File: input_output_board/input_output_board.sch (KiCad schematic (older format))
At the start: 23 parts, among them J1 Neutrik_NCJ6FA-H, J2 Neutrik_NCJ6FA-H, J3 Neutrik_NCJ6FA-H, J4 Neutrik_NCJ6FA-H, J5 AudioJack3, J6 Conn_02x05_Odd_Even, J7 Molex_SL_01x04_Male, J8 Molex_SL_01x04_Male, K1 G6S-2, K2 G6S-2, K3 G6S-2, K4 G6S-2, K5 G6S-2

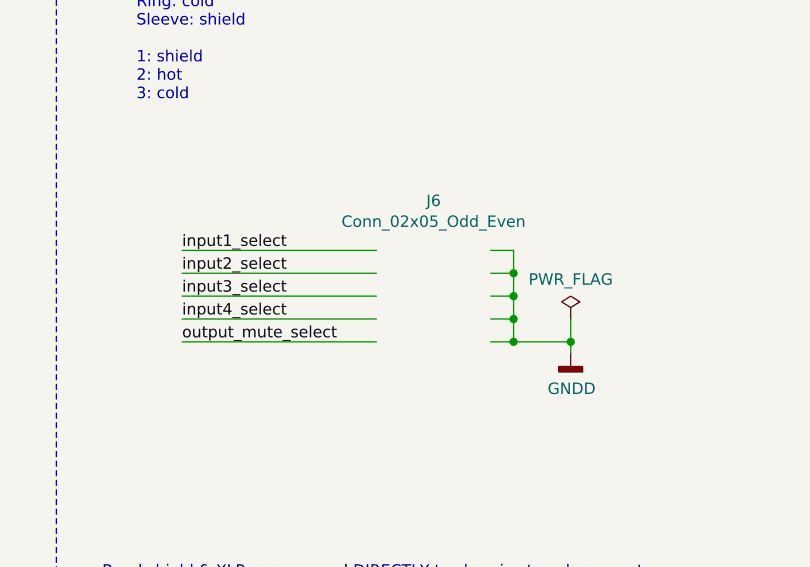
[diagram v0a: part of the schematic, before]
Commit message: complete initial layout
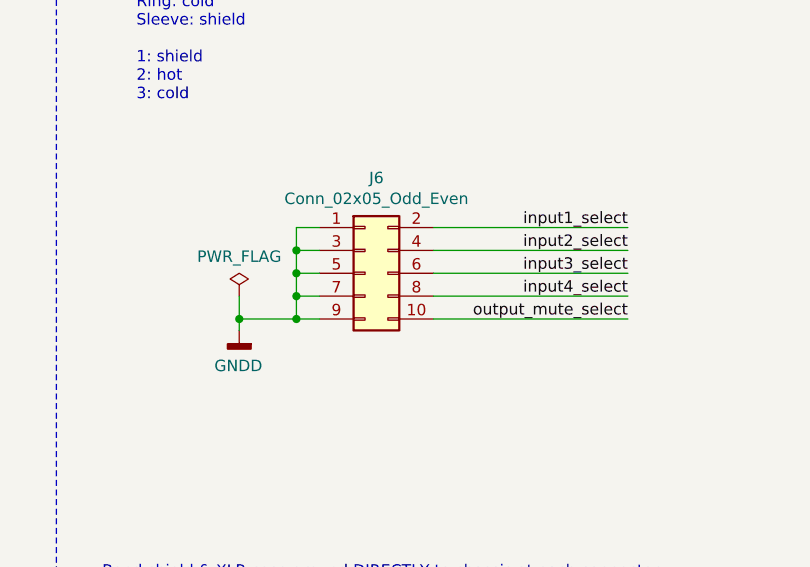
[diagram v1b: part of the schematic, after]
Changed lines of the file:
@@
 NoConn ~ 8400 6150
 NoConn ~ 8400 5750
-Wire Wire Line
-	8800 2350 7950 2350
-Wire Wire Line
-	8800 2450 7950 2450
-Wire Wire Line
-	8800 2550 7950 2550
-Wire Wire Line
-	8800 2650 7950 2650
-Text Label 7950 2350 0    50   ~ 0
+Text Label 9900 2250 2    50   ~ 0
 input1_select
-Text Label 7950 2450 0    50   ~ 0
+Text Label 9900 2350 2    50   ~ 0
 input2_select
-Text Label 7950 2550 0    50   ~ 0
+Text Label 9900 2450 2    50   ~ 0
 input3_select
-Text Label 7950 2650 0    50   ~ 0
+Text Label 9900 2550 2    50   ~ 0
 input4_select
 Wire Wire Line
-	9300 2350 9400 2350
-Wire Wire Line
-	9400 2350 9400 2450
-Wire Wire Line
-	9400 2650 9300 2650
-Wire Wire Line
-	9300 2550 9400 2550
-Connection ~ 9400 2550
-Wire Wire Line
-	9400 2550 9400 2650
-Wire Wire Line
-	9300 2450 9400 2450
-Connection ~ 9400 2450
-Wire Wire Line
-	9400 2450 9400 2550
+	8550 2250 8450 2250
+Wire Wire Line
+	8450 2250 8450 2350
+Wire Wire Line
+	8450 2550 8550 2550
+Wire Wire Line
+	8550 2450 8450 2450
+Connection ~ 8450 2450
+Wire Wire Line
+	8450 2450 8450 2550
+Wire Wire Line
+	8550 2350 8450 2350
+Connection ~ 8450 2350
+Wire Wire Line
+	8450 2350 8450 2450
 $Comp
 L power:GNDD #PWR0101
 U 1 1 5CCCC269
-P 9650 2800
-F 0 "#PWR0101" H 9650 2550 50  0001 C CNN
-F 1 "GNDD" H 9654 2645 50  0000 C CNN
-F 2 "" H 9650 2800 50  0001 C CNN
-F 3 "" H 9650 2800 50  0001 C CNN
-	1    9650 2800
-	1    0    0    -1
-$EndComp
-Wire Wire Line
-	9650 2800 9650 2750
-Wire Wire Line
-	9650 2750 9400 2750
+P 8200 2700
+F 0 "#PWR0101" H 8200 2450 50  0001 C CNN
+F 1 "GNDD" H 8204 2545 50  0000 C CNN
+F 2 "" H 8200 2700 50  0001 C CNN
+F 3 "" H 8200 2700 50  0001 C CNN
+	1    8200 2700
+	-1   0    0    -1
+$EndComp
+Wire Wire Line
+	8200 2700 8200 2650
+Wire Wire Line
+	8200 2650 8450 2650
 $Comp
 L power:GNDD #PWR0103
@@
 Text Label 2900 4700 0    50   ~ 0
 input3_select
-Text Label 7950 2750 0    50   ~ 0
+Text Label 9900 2650 2    50   ~ 0
 output_mute_select
 Wire Wire Line
-	7950 2750 8800 2750
-Wire Wire Line
-	9400 2750 9400 2650
-Connection ~ 9400 2650
-Wire Wire Line
-	9400 2750 9300 2750
-Connection ~ 9400 2750
+	8450 2650 8450 2550
+Connection ~ 8450 2550
+Wire Wire Line
+	8450 2650 8550 2650
+Connection ~ 8450 2650
 Text Label 7350 5250 0    50   ~ 0
 output_mute_select
@@
 L power:PWR_FLAG #FLG0101
 U 1 1 5CD4A6A5
-P 9650 2650
-F 0 "#FLG0101" H 9650 2725 50  0001 C CNN
-F 1 "PWR_FLAG" H 9650 2823 50  0000 C CNN
-F 2 "" H 9650 2650 50  0001 C CNN
-F 3 "~" H 9650 2650 50  0001 C CNN
-	1    9650 2650
-	1    0    0    -1
-$EndComp
-Wire Wire Line
-	9650 2750 9650 2650
-Connection ~ 9650 2750
+P 8200 2550
+F 0 "#FLG0101" H 8200 2625 50  0001 C CNN
+F 1 "PWR_FLAG" H 8200 2723 50  0000 C CNN
+F 2 "" H 8200 2550 50  0001 C CNN
+F 3 "~" H 8200 2550 50  0001 C CNN
+	1    8200 2550
+	-1   0    0    -1
+$EndComp
+Wire Wire Line
+	8200 2650 8200 2550
+Connection ~ 8200 2650
 Text Notes 7600 3950 0    50   ~ 0
 Bond shield & XLR case ground DIRECTLY to chassis at each connector\nflood input_shield across all inputs and connect to input connector (J5)\nMounting holes are for connecting to chassis (via angle bracket)
@@
 	1    0    0    -1
 $EndComp
-$Comp
-L Connector_Generic:Conn_02x05_Odd_Even J6
-U 0 0 5CC54E3F
-P 9000 2550
-F 0 "J6" H 9050 2967 50  0000 C CNN
-F 1 "Conn_02x05_Odd_Even" H 9050 2876 50  0000 C CNN
-F 2 "Connector_Molex_C-Grid:Molex_C-Grid_70246-1001_2x05_P2.54mm_Vertical" H 9000 2550 50  0001 C CNN
-F 3 "~" H 9000 2550 50  0001 C CNN
-	0    9000 2550
-	1    0    0    -1
-$EndComp
 Wire Wire Line
 	5000 3750 5000 4450
@@
 Wire Wire Line
 	5150 4150 5150 5100
+Wire Wire Line
+	9050 2550 9900 2550
+Wire Wire Line
+	9050 2450 9900 2450
+Wire Wire Line
+	9050 2350 9900 2350
+Wire Wire Line
+	9050 2250 9900 2250
+Wire Wire Line
+	9900 2650 9050 2650
+$Comp
+L Connector_Generic:Conn_02x05_Odd_Even J6
+U 1 1 5CC54E3F
+P 8750 2450
+F 0 "J6" H 8800 2867 50  0000 C CNN
+F 1 "Conn_02x05_Odd_Even" H 8800 2776 50  0000 C CNN
+F 2 "Connector_Molex_C-Grid:Molex_C-Grid_70246-1001_2x05_P2.54mm_Vertical" H 8750 2450 50  0001 C CNN
+F 3 "~" H 8750 2450 50  0001 C CNN
+	1    8750 2450
+	1    0    0    -1
+$EndComp
 $EndSCHEMATC

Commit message: update schematic TODO
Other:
- note added: "TODO\ncapacitor(s)\nadd output jack part details\nmounting holes in corners?"
- note removed: "TODO\ncapacitor(s)\nconnector for relay signals -- smaller? more grounds?\nadd Molex C-Grid III symbol & footprint\nadd output jack part details\nmounting holes in corners?"
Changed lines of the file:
@@
 Connection ~ 2050 7350
 Text Notes 7750 950  0    50   ~ 0
-TODO\ncapacitor(s)\nconnector for relay signals -- smaller? more grounds?\nadd Molex C-Grid III symbol & footprint\nadd output jack part details\nmounting holes in corners?
+TODO\ncapacitor(s)\nadd output jack part details\nmounting holes in corners?
 Wire Notes Line
 	7550 4050 10450 4050

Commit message: update chassis grounding in input/output board because jacks connect directly to chassis
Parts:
- removed H1, H2, H3, H4, H5: MountingHole_Pad, MountingHole:MountingHole_3.2mm_M3_Pad_Via, symbol Mechanical:MountingHole_Pad
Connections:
- wire segments 145 -> 140
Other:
- note added: "Shields & XLR case ground bonded DIRECTLY to chassis at each connector:\n - XLR combo connectors via mounting screw holes\n - phono jack via chassis contact\n\nflood input_shield across all inputs and connect to input connector (J7)"
- note added: "TODO\ncapacitor(s)\nadd output jack part details\nmounting holes in corners?\nseparate input shields?"
- note removed: "Bond shield & XLR case ground DIRECTLY to chassis at each connector\nflood input_shield across all inputs and connect to input connector (J5)\nMounting holes are for connecting to chassis (via angle bracket)"
- note removed: "TODO\ncapacitor(s)\nadd output jack part details\nmounting holes in corners?"
- moved on the sheet: J1B
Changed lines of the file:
@@
 output_shield
 Wire Wire Line
-	2050 1600 1450 1600
-Wire Wire Line
-	1450 1500 2050 1500
+	2000 1600 1400 1600
+Wire Wire Line
+	1400 1500 2000 1500
 $Comp
 L Device:D D3
@@
 Text Label 2000 5000 2    50   ~ 0
 input3_hot
-Text Label 2050 1700 2    50   ~ 0
+Text Label 2000 1700 2    50   ~ 0
 input_shield
-Text Label 2050 1600 2    50   ~ 0
+Text Label 2000 1600 2    50   ~ 0
 input1_cold
-Text Label 2050 1500 2    50   ~ 0
+Text Label 2000 1500 2    50   ~ 0
 input1_hot
 $Comp
@@
 	7300 5550 8400 5550
 Wire Wire Line
-	8050 5750 8050 6400
-Wire Wire Line
-	8050 6400 9300 6400
-Wire Wire Line
-	9300 6400 9300 5850
+	8050 5750 8050 6350
+Wire Wire Line
+	8050 6350 9300 6350
+Wire Wire Line
+	9300 6350 9300 5850
 Wire Wire Line
 	9300 5850 9400 5850
@@
 	8200 2650 8200 2550
 Connection ~ 8200 2650
-Text Notes 7600 3950 0    50   ~ 0
-Bond shield & XLR case ground DIRECTLY to chassis at each connector\nflood input_shield across all inputs and connect to input connector (J5)\nMounting holes are for connecting to chassis (via angle bracket)
-$Comp
-L Mechanical:MountingHole_Pad H2
-U 1 1 5CD65332
-P 1800 3850
-F 0 "H2" V 1846 3999 50  0000 L CNN
-F 1 "MountingHole_Pad" V 1755 3999 50  0000 L CNN
-F 2 "MountingHole:MountingHole_3.2mm_M3_Pad_Via" H 1800 3850 50  0001 C CNN
-F 3 "~" H 1800 3850 50  0001 C CNN
-	1    1800 3850
-	0    -1   -1   0
-$EndComp
-$Comp
-L Mechanical:MountingHole_Pad H3
-U 1 1 5CD66551
-P 1800 5600
-F 0 "H3" V 1846 5749 50  0000 L CNN
-F 1 "MountingHole_Pad" V 1755 5749 50  0000 L CNN
-F 2 "MountingHole:MountingHole_3.2mm_M3_Pad_Via" H 1800 5600 50  0001 C CNN
-F 3 "~" H 1800 5600 50  0001 C CNN
-	1    1800 5600
-	0    -1   -1   0
-$EndComp
-Wire Wire Line
-	9300 6400 9400 6400
-Connection ~ 9300 6400
-$Comp
-L Mechanical:MountingHole_Pad H5
-U 1 1 5CD67130
-P 9500 6400
-F 0 "H5" V 9454 6550 50  0000 L CNN
-F 1 "MountingHole_Pad" V 9545 6550 50  0000 L CNN
-F 2 "MountingHole:MountingHole_3.2mm_M3_Pad_Via" H 9500 6400 50  0001 C CNN
-F 3 "~" H 9500 6400 50  0001 C CNN
-	1    9500 6400
-	0    1    1    0
-$EndComp
+Text Notes 7500 3950 0    50   ~ 0
+Shields & XLR case ground bonded DIRECTLY to chassis at each connector:\n - XLR combo connectors via mounting screw holes\n - phono jack via chassis contact\n\nflood input_shield across all inputs and connect to input connector (J7)
 Wire Wire Line
 	2350 2100 2350 2000
 Wire Wire Line
-	2100 1700 2100 2100
-Wire Wire Line
-	2100 1700 2150 1700
-Wire Wire Line
-	2100 2100 2350 2100
-$Comp
-L Mechanical:MountingHole_Pad H1
-U 1 1 5CD64CD4
-P 1800 2100
-F 0 "H1" V 1846 2249 50  0000 L CNN
-F 1 "MountingHole_Pad" V 1755 2249 50  0000 L CNN
-F 2 "MountingHole:MountingHole_3.2mm_M3_Pad_Via" H 1800 2100 50  0001 C CNN
-F 3 "~" H 1800 2100 50  0001 C CNN
-	1    1800 2100
-	0    -1   -1   0
-$EndComp
+	2050 1700 2050 2100
+Wire Wire Line
+	2050 2100 2350 2100
 Wire Wire Line
 	2350 3750 2350 3850
@@
 Wire Wire Line
 	2050 3450 2150 3450
-Connection ~ 2050 3850
-Wire Wire Line
-	1900 3850 2050 3850
-Wire Wire Line
-	1900 5600 2050 5600
 Wire Wire Line
 	2350 5600 2350 5500
@@
 	2050 5200 2050 5600
 Connection ~ 2050 5200
-Connection ~ 2050 5600
 Wire Wire Line
 	2050 5600 2350 5600
 Wire Wire Line
-	1900 2100 2100 2100
-Connection ~ 2100 2100
-Wire Wire Line
 	2050 6950 2150 6950
 Wire Wire Line
@@
 Wire Wire Line
 	2050 7350 2350 7350
-$Comp
-L Mechanical:MountingHole_Pad H4
-U 1 1 5CD66BD9
-P 1800 7350
-F 0 "H4" V 1846 7499 50  0000 L CNN
-F 1 "MountingHole_Pad" V 1755 7499 50  0000 L CNN
-F 2 "MountingHole:MountingHole_3.2mm_M3_Pad_Via" H 1800 7350 50  0001 C CNN
-F 3 "~" H 1800 7350 50  0001 C CNN
-	1    1800 7350
-	0    -1   -1   0
-$EndComp
 Text Label 2000 6950 2    50   ~ 0
 input_shield
@@
 	2000 6750 1400 6750
 Wire Wire Line
-	2050 6950 1400 6950
-Wire Wire Line
 	2000 6850 1400 6850
 Text Label 2000 6850 2    50   ~ 0
@@
 Text Label 2900 5600 0    50   ~ 0
 input3_cold
-Wire Wire Line
-	1400 5200 2050 5200
 Text Label 2000 3350 2    50   ~ 0
 input2_cold
@@
 Wire Wire Line
 	2000 3250 1400 3250
-Wire Wire Line
-	2050 3450 1400 3450
 Connection ~ 2050 3450
 Wire Wire Line
@@
 Wire Wire Line
 	2450 2100 3700 2100
-Wire Wire Line
-	1450 1700 2100 1700
-Connection ~ 2100 1700
-Wire Wire Line
-	1900 7350 2050 7350
-Connection ~ 2050 7350
 Text Notes 7750 950  0    50   ~ 0
-TODO\ncapacitor(s)\nadd output jack part details\nmounting holes in corners?
+TODO\ncapacitor(s)\nadd output jack part details\nmounting holes in corners?\nseparate input shields?
 Wire Notes Line
 	7550 4050 10450 4050
@@
 L Connector_gkeeth:Neutrik_NCJ6FA-H J1
 U 2 1 5CEE74AE
-P 1250 1600
-F 0 "J1" H 1232 1233 50  0000 C CNN
-F 1 "Neutrik_NCJ6FA-H" H 1232 1324 50  0000 C CNN
-F 2 "Connector_Audio_gkeeth:Jack_Combo_Neutrik_NCJ6FA-H_Horizontal" H 1250 1600 50  0001 C CNN
-F 3 "https://www.neutrik.com/media/8445/download/ncj6fa-v.pdf?v=1" H 1250 1600 50  0001 C CNN
-F 4 "Neutrik" H 1250 1600 50  0001 C CNN "Manufacturer"
-F 5 "NCJ6FA-H" H 1250 1600 50  0001 C CNN "Manufacturer PN"
-F 6 "Mouser" H 1250 1600 50  0001 C CNN "Distributor"
-F 7 "568-NCJ6FA-H" H 1250 1600 50  0001 C CNN "Distributor PN"
-F 8 "https://www.mouser.com/ProductDetail/Neutrik/NCJ6FA-H?qs=aEaV1LakhLZ1UcG8BF7YQQ%3D%3D" H 1250 1600 50  0001 C CNN "URL"
-F 9 "2.10" H 1250 1600 50  0001 C CNN "Unit Price"
-	2    1250 1600
+P 1200 1600
+F 0 "J1" H 1182 1233 50  0000 C CNN
+F 1 "Neutrik_NCJ6FA-H" H 1182 1324 50  0000 C CNN
+F 2 "Connector_Audio_gkeeth:Jack_Combo_Neutrik_NCJ6FA-H_Horizontal" H 1200 1600 50  0001 C CNN
+F 3 "https://www.neutrik.com/media/8445/download/ncj6fa-v.pdf?v=1" H 1200 1600 50  0001 C CNN
+F 4 "Neutrik" H 1200 1600 50  0001 C CNN "Manufacturer"
+F 5 "NCJ6FA-H" H 1200 1600 50  0001 C CNN "Manufacturer PN"
+F 6 "Mouser" H 1200 1600 50  0001 C CNN "Distributor"
+F 7 "568-NCJ6FA-H" H 1200 1600 50  0001 C CNN "Distributor PN"
+F 8 "https://www.mouser.com/ProductDetail/Neutrik/NCJ6FA-H?qs=aEaV1LakhLZ1UcG8BF7YQQ%3D%3D" H 1200 1600 50  0001 C CNN "URL"
+F 9 "2.10" H 1200 1600 50  0001 C CNN "Unit Price"
+	2    1200 1600
 	1    0    0    1
 $EndComp
@@
 	1    0    0    -1
 $EndComp
+Connection ~ 2050 1700
+Wire Wire Line
+	2050 1700 2150 1700
+Wire Wire Line
+	1400 5200 2050 5200
+Wire Wire Line
+	1400 6950 2050 6950
+Wire Wire Line
+	1400 3450 2050 3450
+Wire Wire Line
+	1400 1700 2050 1700
 $EndSCHEMATC

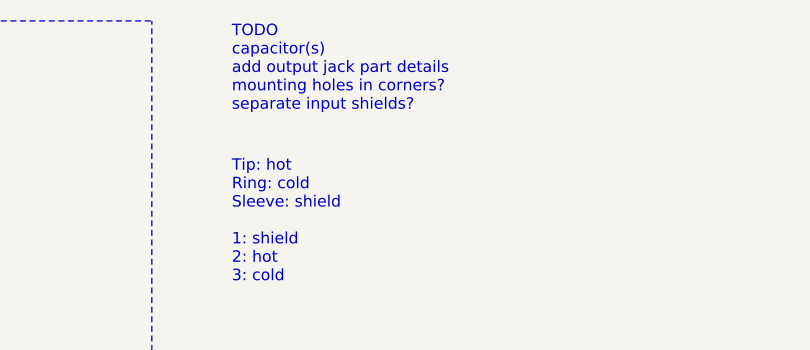
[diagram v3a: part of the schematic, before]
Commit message: add part details for output jack (NRJ3HF-1) and update TODO list
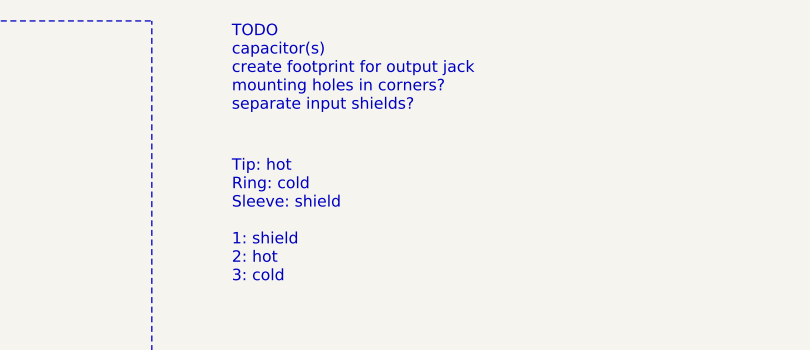
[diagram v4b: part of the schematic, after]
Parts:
- J5: Distributor (none) -> Mouser; Distributor PN (none) -> 568-NRJ3HF-1; Manufacturer (none) -> Neutrik; Manufacturer PN (none) -> NRJ3HF-1; URL (none) -> https://www.mouser.com/ProductDetail/568-NRJ3HF-1; Unit Price (none) -> 0.63
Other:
- note added: "TODO\ncapacitor(s)\ncreate footprint for output jack\nmounting holes in corners?\nseparate input shields?"
- note removed: "TODO\ncapacitor(s)\nadd output jack part details\nmounting holes in corners?\nseparate input shields?"
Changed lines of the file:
@@
 F 1 "AudioJack3" H 9320 5684 50  0000 R CNN
 F 2 "Connector_Audio:Jack_3.5mm_Neutrik_NMJ6HCD2_Horizontal" H 9600 5750 50  0001 C CNN
-F 3 "~" H 9600 5750 50  0001 C CNN
+F 3 "https://www.neutrik.us/media/8560/download/nrj3hf-1-2.pdf?v=1" H 9600 5750 50  0001 C CNN
+F 4 "Neutrik" H 9600 5750 50  0001 C CNN "Manufacturer"
+F 5 "NRJ3HF-1" H 9600 5750 50  0001 C CNN "Manufacturer PN"
+F 6 "Mouser" H 9600 5750 50  0001 C CNN "Distributor"
+F 7 "568-NRJ3HF-1" H 9600 5750 50  0001 C CNN "Distributor PN"
+F 8 "https://www.mouser.com/ProductDetail/568-NRJ3HF-1" H 9600 5750 50  0001 C CNN "URL"
+F 9 "0.63" H 9600 5750 50  0001 C CNN "Unit Price"
 	1    9600 5750
 	-1   0    0    1
@@
 	2450 2100 3700 2100
 Text Notes 7750 950  0    50   ~ 0
-TODO\ncapacitor(s)\nadd output jack part details\nmounting holes in corners?\nseparate input shields?
+TODO\ncapacitor(s)\ncreate footprint for output jack\nmounting holes in corners?\nseparate input shields?
 Wire Notes Line
 	7550 4050 10450 4050

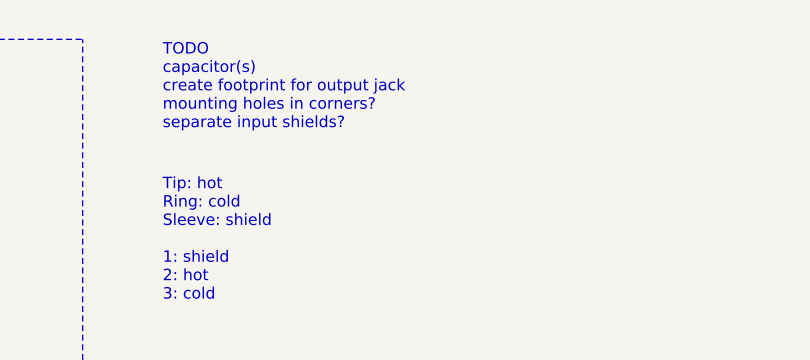
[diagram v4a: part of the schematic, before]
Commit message: update todo for input output board
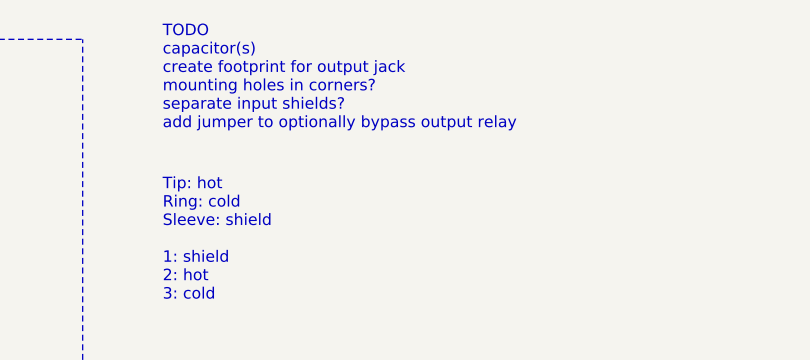
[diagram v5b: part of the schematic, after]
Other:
- note added: "TODO\ncapacitor(s)\ncreate footprint for output jack\nmounting holes in corners?\nseparate input shields?\nadd jumper to optionally bypass output relay"
- note removed: "TODO\ncapacitor(s)\ncreate footprint for output jack\nmounting holes in corners?\nseparate input shields?"
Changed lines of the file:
@@
 	2450 2100 3700 2100
 Text Notes 7750 950  0    50   ~ 0
-TODO\ncapacitor(s)\ncreate footprint for output jack\nmounting holes in corners?\nseparate input shields?
+TODO\ncapacitor(s)\ncreate footprint for output jack\nmounting holes in corners?\nseparate input shields?\nadd jumper to optionally bypass output relay
 Wire Notes Line
 	7550 4050 10450 4050
